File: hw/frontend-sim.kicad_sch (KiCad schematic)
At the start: 12 parts

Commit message: Filter calc checkpoint
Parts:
- removed R7729, R7732: 50, symbol Device:R_US
- removed V7703: VSIN, symbol Simulation_SPICE:VSIN
- added R7748, R7749: 50, symbol Device:R_US
- added V7705: VSIN, symbol Simulation_SPICE:VSIN
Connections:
- net GND: now also R7749.2, V7705.2
- new net: R7748.1, V7705.1
- new net test/ladderIn: R7748.2
- new net vLadderOut: R7749.1
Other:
- sheet test ports: added ladderIn, ladderOut; removed acIn, acOut

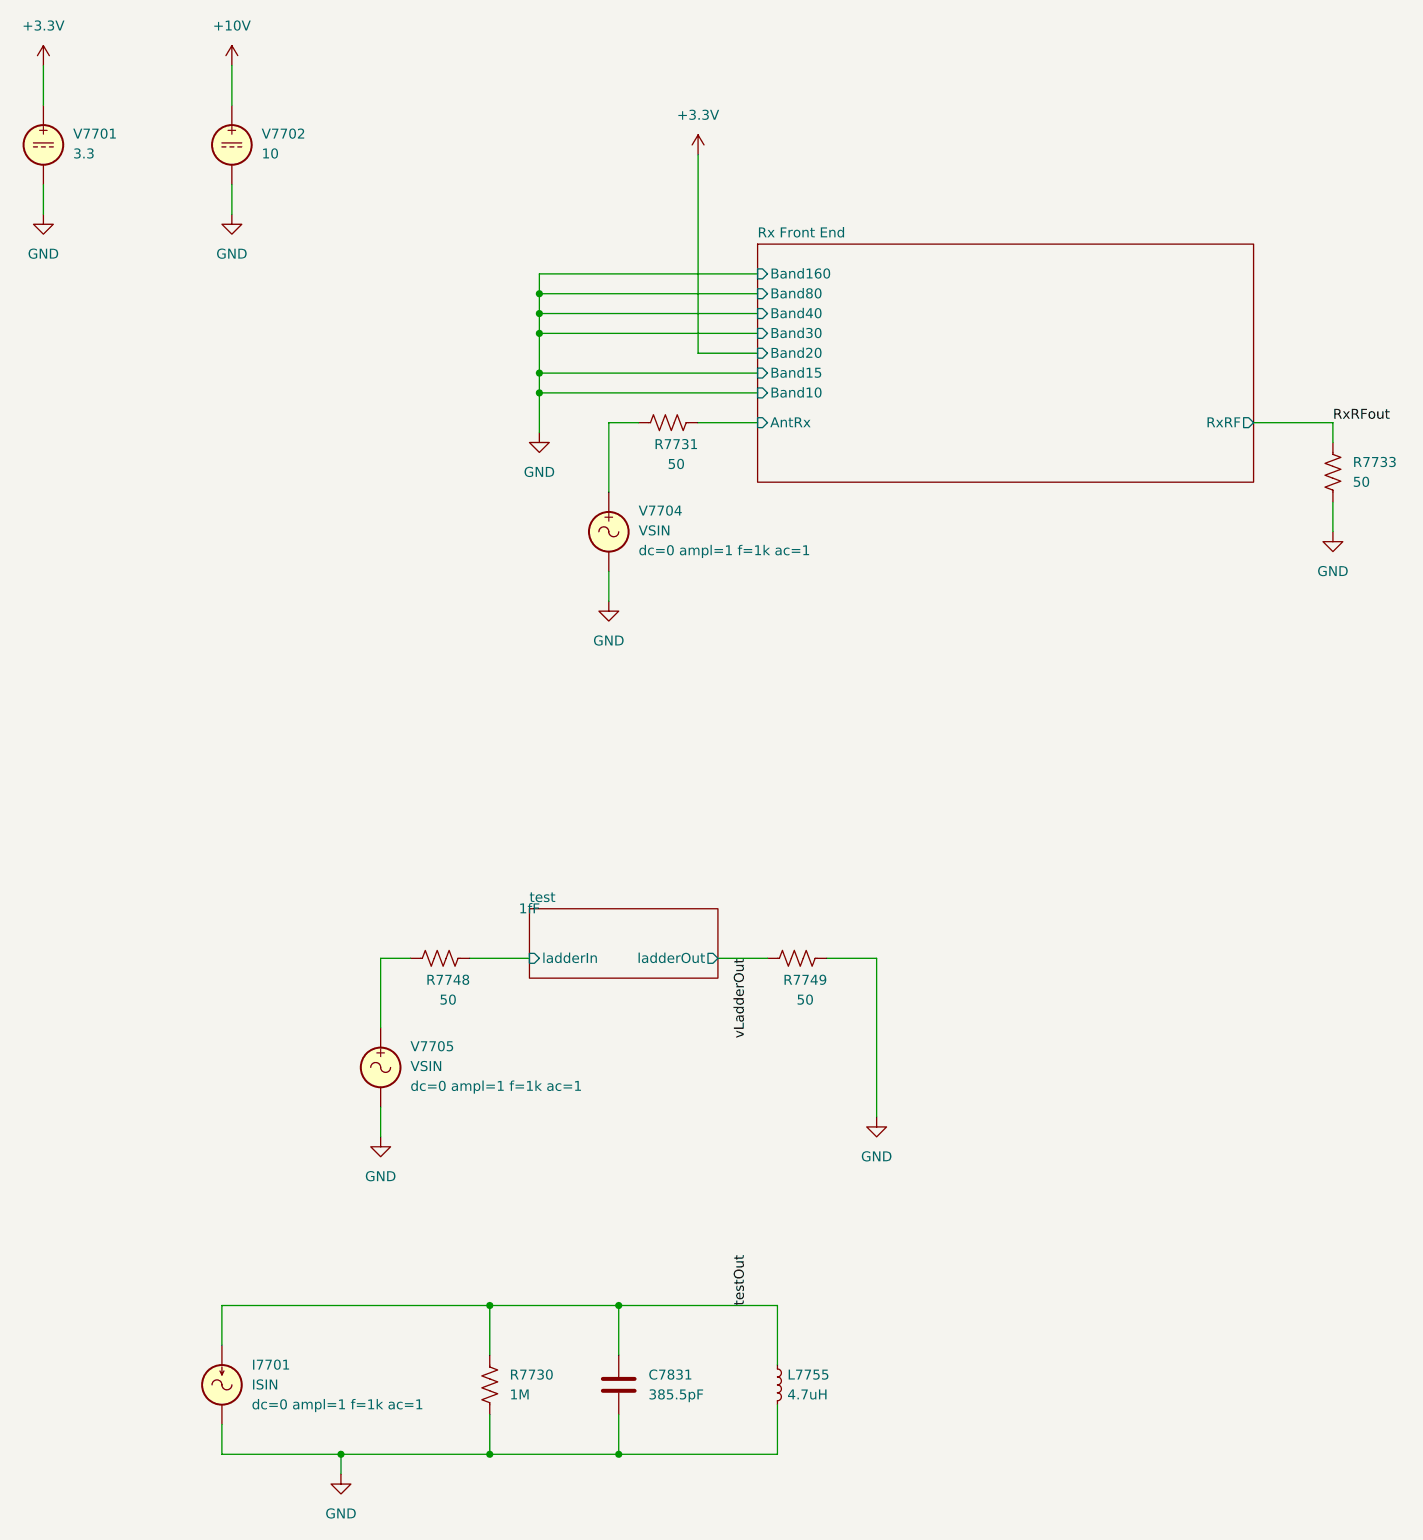
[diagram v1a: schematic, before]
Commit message: Getting closer to having all (ten) BPFs designed. Maybe I can try some layout next.
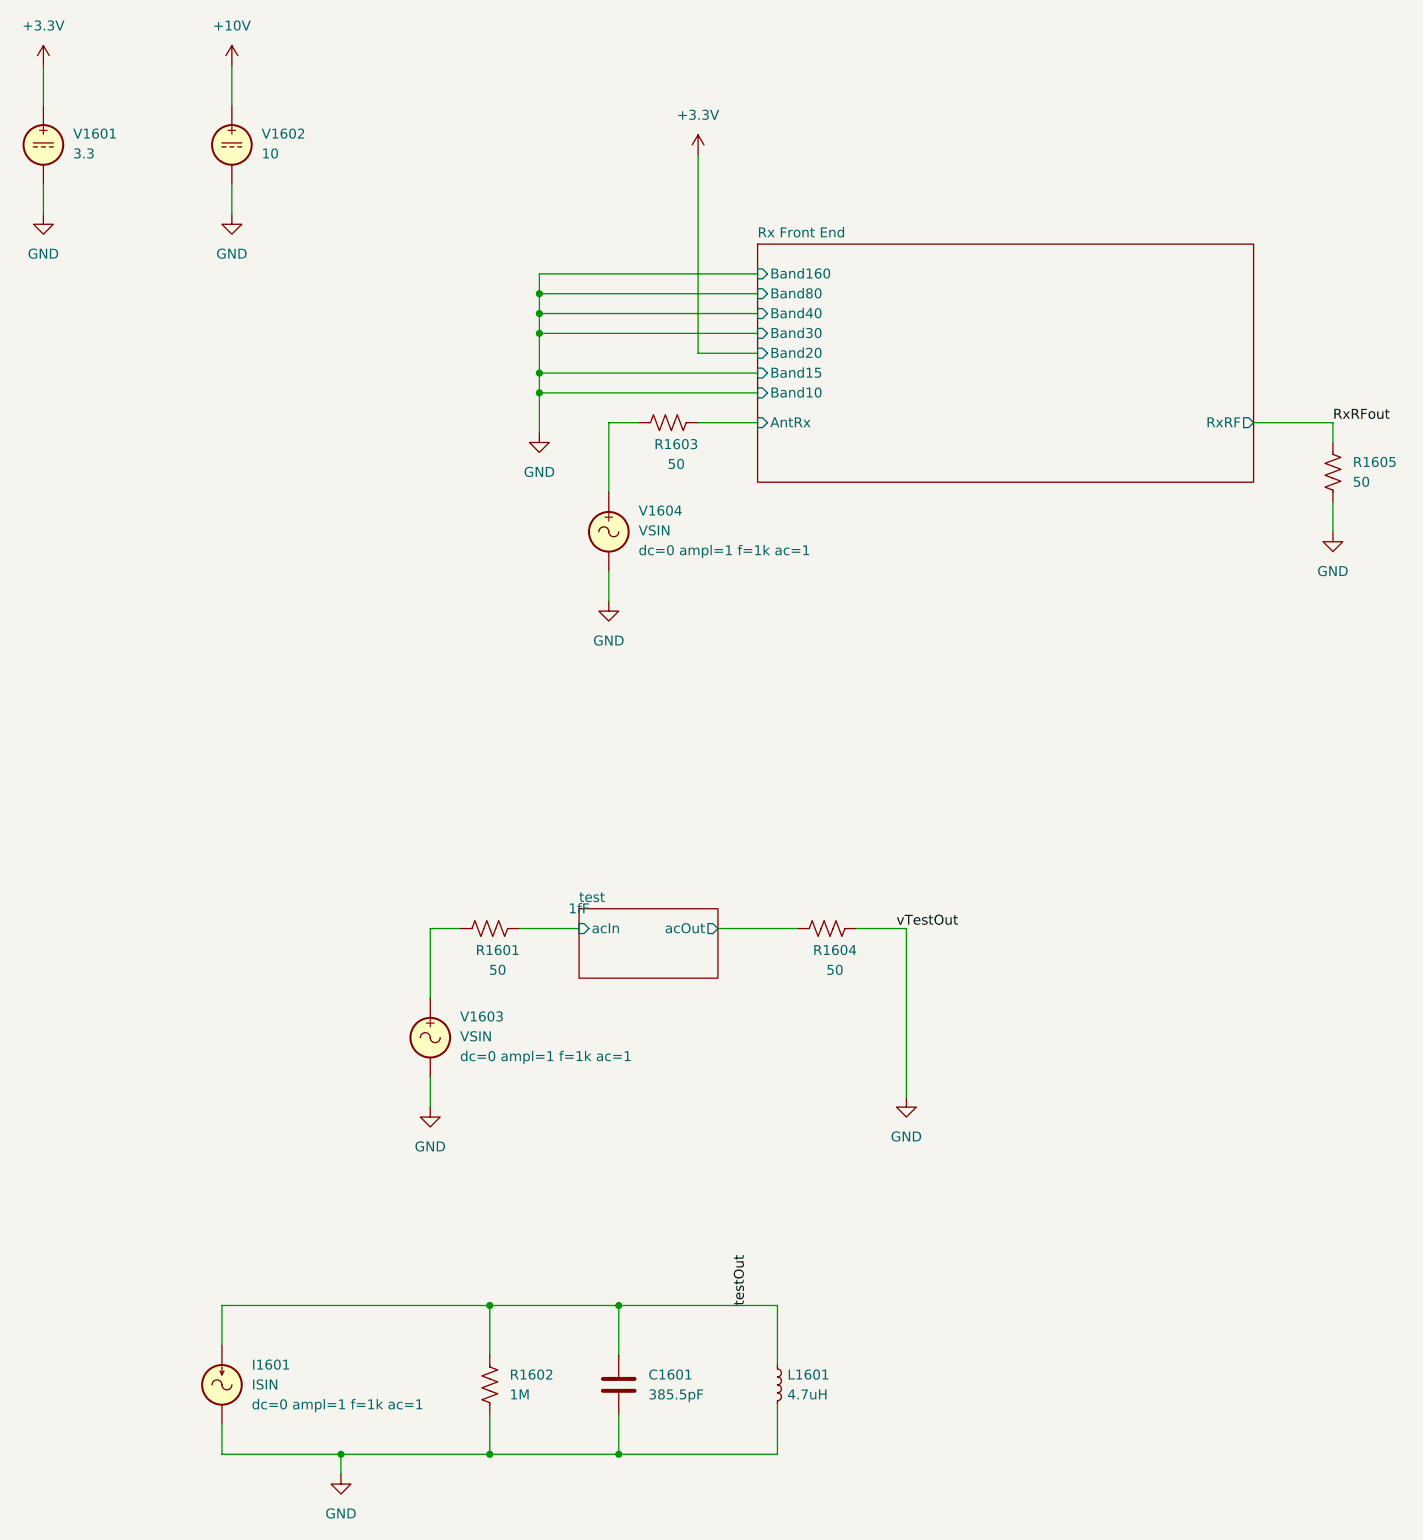
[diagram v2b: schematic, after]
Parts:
- removed R7748, R7749: 50, symbol Device:R_US
- removed V7705: VSIN, symbol Simulation_SPICE:VSIN
- added R1601, R1604: 50, symbol Device:R_US
- added V1603: VSIN, symbol Simulation_SPICE:VSIN
- renumbered C7831 to C1601, I7701 to I1601, L7755 to L1601, R7730 to R1602, R7731 to R1603, R7733 to R1605, V7701 to V1601, V7702 to V1602, V7704 to V1604
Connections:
- net GND: now also R1604.2, V1603.2
- new net: R1601.1, V1603.1
- new net test/acIn: R1601.2
- new net test/acOut: R1604.1
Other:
- sheet test ports: added acIn, acOut; removed ladderIn, ladderOut
